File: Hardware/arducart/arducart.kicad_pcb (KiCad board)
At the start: 2 copper layers, 53 x 39.2 mm, 11 parts, among them J2 AVR-ISP-6

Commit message: First routing
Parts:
- R2, R3, R4, R5, R6, R7, R8: moved to B.Cu
- moved R3 26.2 mm to (146.9, 78.0), turned to 90 degrees
- moved R2 24.1 mm to (141.9, 83.8), turned to -90 degrees
- moved R4 23.5 mm to (144.4, 78.0), turned to 90 degrees
- moved R5 21.2 mm to (141.9, 78.0), turned to 90 degrees
- moved R1 20.5 mm to (118.4, 88.8), turned to -90 degrees
- moved R6 19.7 mm to (139.3, 78.0), turned to 90 degrees
- moved R7 18.9 mm to (139.3, 83.8), turned to -90 degrees
- moved R8 15.4 mm to (134.2, 83.8), turned to -90 degrees
- moved J2 3.23 mm to (161.7, 82.1)
- moved U1 1.01 mm to (141.9, 80.9), turned to 90 degrees
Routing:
- net GND: track 0.00 -> 157.3 mm, vias 0 -> 5
- net VCC: track 0.00 -> 84.2 mm, vias 0 -> 1
- net ISP_SCK: track 0.00 -> 80.4 mm
- net ISP_MOSI: track 0.00 -> 71.7 mm
- net BTN_UP: track 0.00 -> 45.8 mm
- net BTN_DOWN: track 0.00 -> 41.0 mm, vias 0 -> 1
- net ISP_RST: track 0.00 -> 40.3 mm
- net BTN_RIGHT: track 0.00 -> 32.3 mm, vias 0 -> 1
- net BTN_LEFT: track 0.00 -> 32.3 mm
- net SPI_CS: track 0.00 -> 32.0 mm, vias 0 -> 2
- net SCREEN_DC: track 0.00 -> 28.3 mm
- net BUZZER: track 0.00 -> 28.0 mm
- net Net-(J1-BTN_MENU1): track 0.00 -> 25.8 mm, vias 0 -> 2
- net SCREEN_RESET: track 0.00 -> 23.6 mm
- net BTN_B: track 0.00 -> 21.1 mm, vias 0 -> 2
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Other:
- board size 53 x 39.2 mm -> 53 x 36.2 mm

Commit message: Finish PCB design
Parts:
- moved J2 1.50 mm to (160.9, 80.9)
- moved R2 1.27 mm to (141.9, 82.5)
- moved R3 1.27 mm to (146.9, 76.7)
- moved R4 1.27 mm to (144.4, 76.7)
- moved R5 1.27 mm to (141.9, 76.7)
- moved R6 1.27 mm to (139.3, 76.7)
- moved R8 1.27 mm to (134.2, 82.6)
- moved U1 1.27 mm to (141.9, 79.6)
- moved R1 1.27 mm to (118.4, 87.5)
- moved R7 1.27 mm to (139.3, 82.5)
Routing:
- net BTN_A: track 19.1 -> 43.8 mm, vias 0 -> 1
- net BTN_B: track 21.1 -> 41.1 mm, vias 2 -> 5
- net ISP_MOSI: track 71.7 -> 78.7 mm
- net GND: track 157.3 -> 164.1 mm
- net ISP_SCK: track 80.4 -> 83.9 mm
- net BTN_UP: track 45.8 -> 48.8 mm
- net BTN_LEFT: track 32.3 -> 35.1 mm
- net SCREEN_RESET: track 23.6 -> 25.9 mm
- net SCREEN_DC: track 28.3 -> 30.2 mm
- net BTN_RIGHT: track 32.3 -> 34.1 mm
- net ISP_MISO: track 21.1 -> 19.5 mm
- net Net-(J1-BTN_MENU1): track 25.8 -> 27.1 mm
- net BUZZER: track 28.0 -> 29.2 mm
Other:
- board size 53 x 36.2 mm -> 53 x 37.5 mm
- board text added: "1"
- board text added: "30"
- board text added: "ArduCard v0.1"
- board text added: "MISO"
- board text added: "MOSI"
- board text added: "RST"
- board text added: "SCK"
- board text added: "VCC"

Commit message: Add logo on PCBs
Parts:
- added REF**: Logo, carts:Logo, F.Cu at (122.8, 75.8)
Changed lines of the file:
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@@
 		)
+	)
+	(footprint "carts:Logo"
+		(layer "F.Cu")
+		(at 122.75 75.75)
+		(property "Reference" "REF**"
+			(at 0 -5.08 0)
+			(unlocked yes)
+			(layer "F.SilkS")
+			(hide yes)
+			(effects
+				(font
+					(size 1 1)
+					(thickness 0.1)
+				)
+			)
+		)
+		(property "Value" "Logo"
+			(at 0 5.08 0)
+			(unlocked yes)
+			(layer "F.Fab")
+			(hide yes)
+			(effects
+				(font
+					(size 1 1)
+					(thickness 0.15)
+				)
+			)
+		)
+		(property "Datasheet" ""
+			(at 0 0 0)
+			(unlocked yes)
+			(layer "F.Fab")
+			(hide yes)
+			(effects
+				(font
+					(size 1 1)
+					(thickness 0.15)
+				)
+			)
+		)
+		(property "Description" ""
+			(at 0 0 0)
+			(unlocked yes)
+			(layer "F.Fab")
+			(hide yes)
+			(effects
+				(font
+					(size 1 1)
+					(thickness 0.15)
+				)
+			)
+		)
+		(attr smd)
+		(fp_line
+			(start -1 -2.75)
+			(end 0 -2.75)
+			(stroke
+				(width 1)
+				(type default)
+			)
+			(layer "F.SilkS")
+		)
+		(fp_line
+			(start -1 -0.25)
+			(end -1 0.5)
+			(stroke
+				(width 0.5)
+				(type default)
+			)
+			(layer "F.SilkS")
+		)
+		(fp_line
+			(start 1.5 1.25)
+			(end 1.5 -2.75)
+			(stroke
+				(width 1)
+				(type default)
+			)
+			(layer "F.SilkS")
+		)
+		(fp_line
+			(start 2 -0.75)
+			(end -0.5 -0.75)
+			(stroke
+				(width 0.5)
+				(type default)
+			)
+			(layer "F.SilkS")
+		)
+		(fp_line
+			(start 3.5 -2.75)
+			(end 1.5 -2.75)
+			(stroke
+				(width 1)
+				(type default)
+			)
+			(layer "F.SilkS")
+		)
+		(fp_line
+			(start 3.5 -0.75)
+			(end 1.5 -0.75)
+			(stroke
+				(width 1)
+				(type default)
+			)
+			(layer "F.SilkS")
+		)
+		(fp_line
+			(start 3.5 1.25)
+			(end 1.5 1.25)
+			(stroke
+				(width 1)
+				(type default)
+			)
+			(layer "F.SilkS")
+		)
+		(fp_line
+			(start 3.5 2.75)
+			(end -1 2.75)
+			(stroke
+				(width 1)
+				(type default)
+			)
+			(layer "F.SilkS")
+		)
+		(fp_arc
+			(start -1 2.75)
+			(mid -3.75 0)
+			(end -1 -2.75)
+			(stroke
+				(width 1)
+				(type default)
+			)
+			(layer "F.SilkS")
+		)
+		(fp_circle
+			(center -1 -0.75)
+			(end -0.5 -0.75)
+			(stroke
+				(width 0.5)
+				(type solid)
+			)
+			(fill no)
+			(layer "F.SilkS")
+		)
+		(fp_circle
+			(center -1 1)
+			(end -0.5 1)
+			(stroke
+				(width 0.5)
+				(type solid)
+			)
+			(fill no)
+			(layer "F.SilkS")
+		)
+		(fp_rect
+			(start -4.25 -3.25)
+			(end 4 3.25)
+			(stroke
+				(width 0.1)
+				(type solid)
+			)
+			(fill no)
+			(layer "F.CrtYd")
+		)
+		(fp_text user "${REFERENCE}"
+			(at -0.25 -4.25 0)
+			(unlocked yes)
+			(layer "F.Fab")
+			(effects
+				(font
+					(size 1 1)
+					(thickness 0.15)
+				)
+			)
+		)
+		(embedded_fonts no)
 	)
 	(footprint "carts:Edge_Connector"

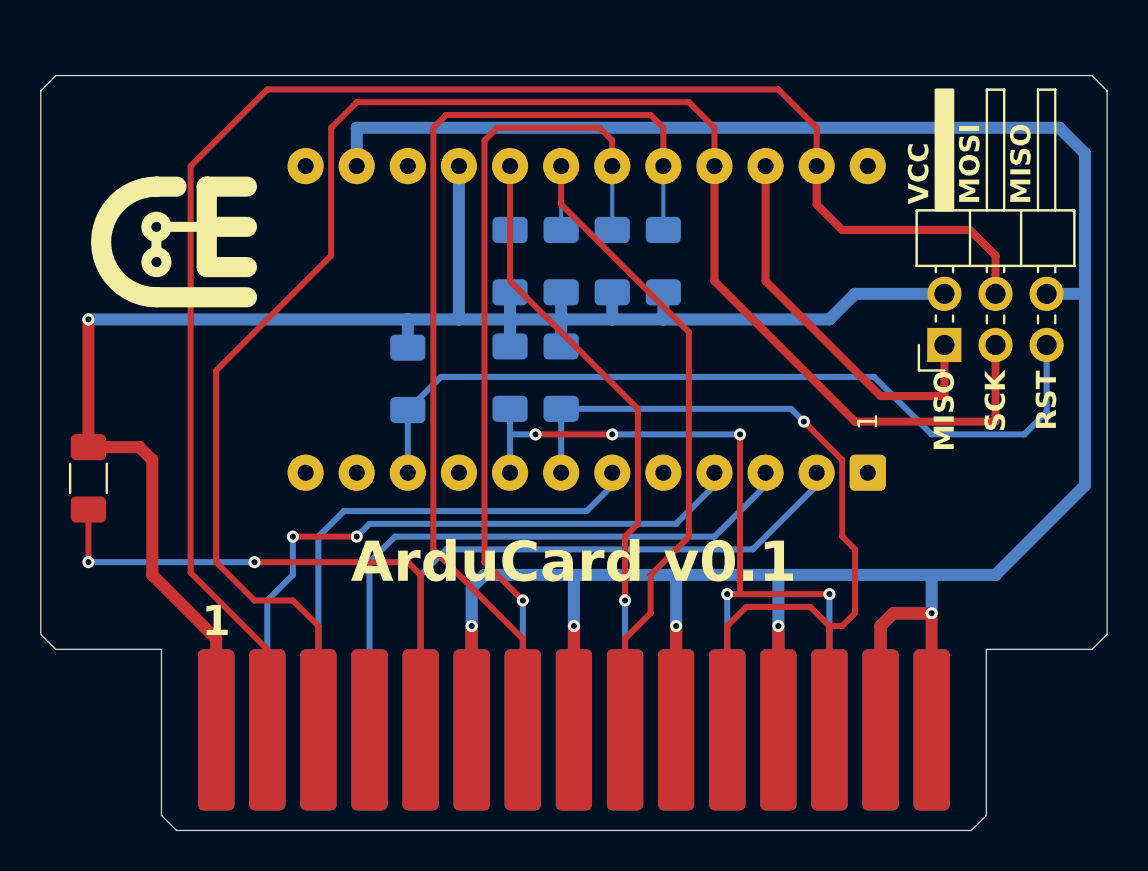
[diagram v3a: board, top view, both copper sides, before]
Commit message: Add holes, add space for cartrige case
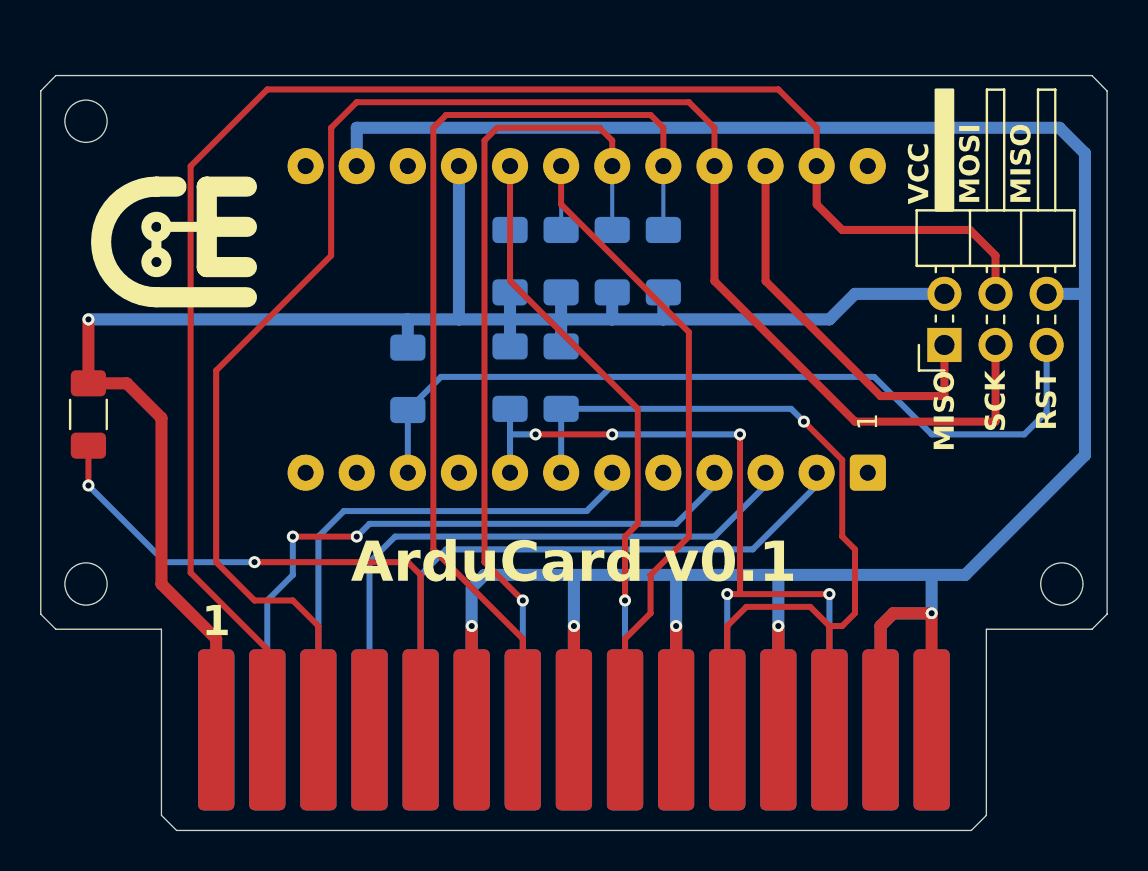
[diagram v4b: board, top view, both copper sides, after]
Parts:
- added REF**: MountingHole_2.1mm, MountingHole:MountingHole_2.1mm, F.Cu at (118.2, 92.8)
- added REF**: MountingHole_2.1mm, MountingHole:MountingHole_2.1mm, F.Cu at (118.2, 69.8)
- added REF**: MountingHole_2.1mm, MountingHole:MountingHole_2.1mm, F.Cu at (166.8, 92.8)
- moved R1 3.17 mm to (118.4, 84.3)
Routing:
- net Net-(J1-BTN_MENU1): track 27.1 -> 28.0 mm
- net GND: track 164.1 -> 163.2 mm
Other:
- outline, holes or cut-outs redrawn

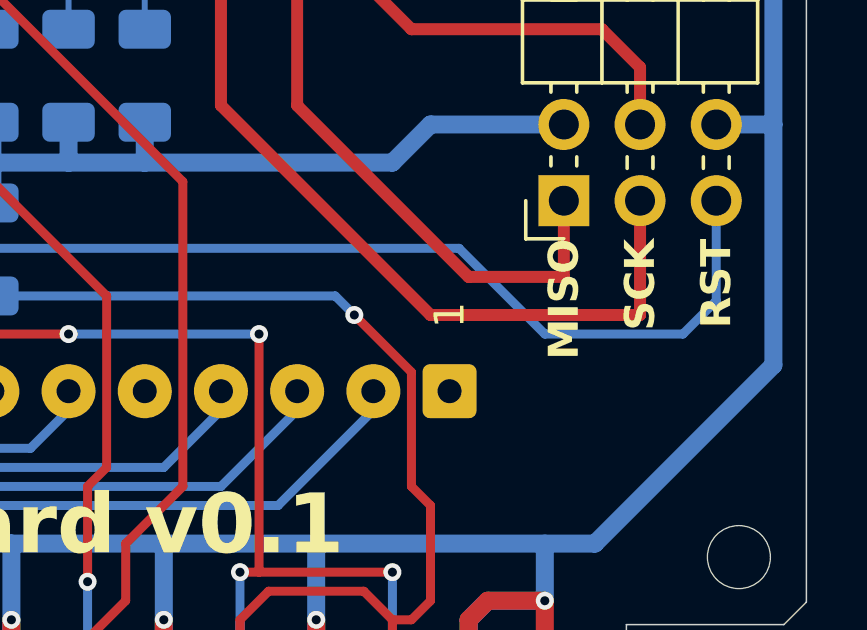
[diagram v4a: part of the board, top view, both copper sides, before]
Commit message: Fixes to comply to design rules
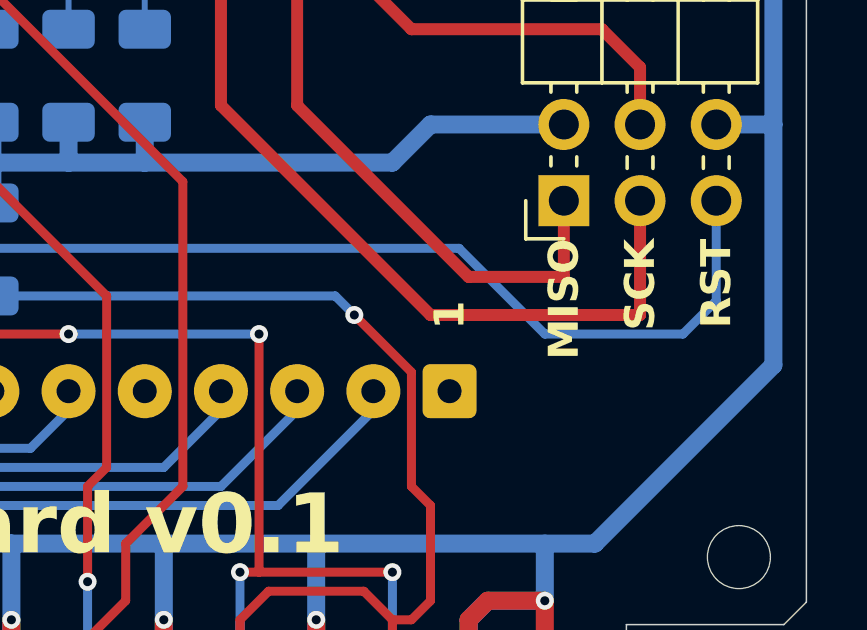
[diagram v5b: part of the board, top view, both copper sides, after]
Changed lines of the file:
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@@
 	)
 	(setup
+		(stackup
+			(layer "F.SilkS"
+				(type "Top Silk Screen")
+			)
+			(layer "F.Paste"
+				(type "Top Solder Paste")
+			)
+			(layer "F.Mask"
+				(type "Top Solder Mask")
+				(thickness 0.01)
+			)
+			(layer "F.Cu"
+				(type "copper")
+				(thickness 0.035)
+			)
+			(layer "dielectric 1"
+				(type "core")
+				(thickness 1.51)
+				(material "FR4")
+				(epsilon_r 4.5)
+				(loss_tangent 0.02)
+			)
+			(layer "B.Cu"
+				(type "copper")
+				(thickness 0.035)
+			)
+			(layer "B.Mask"
+				(type "Bottom Solder Mask")
+				(thickness 0.01)
+			)
+			(layer "B.Paste"
+				(type "Bottom Solder Paste")
+			)
+			(layer "B.SilkS"
+				(type "Bottom Silk Screen")
+			)
+			(copper_finish "None")
+			(dielectric_constraints no)
+		)
 		(pad_to_mask_clearance 0)
 		(allow_soldermask_bridges_in_footprints no)
@@
 		(sheetfile "arducart.kicad_sch")
 		(attr through_hole)
-		(fp_poly
-			(pts
-				(xy -9.274999 -16.8) (xy 9.274999 -16.8) (xy 9.274999 16.8) (xy -9.274999 16.8)
-			)
+		(fp_rect
+			(start -9.275 -16.8)
+			(end 9.275 16.8)
 			(stroke
 				(width 0.1)
@@
 				(font
 					(size 1 1)
-					(thickness 0.1)
+					(thickness 0.2)
+					(bold yes)
 				)
 			)
@@
 			(layer "F.SilkS")
 		)
-		(fp_rect
-			(start -4.25 -3.25)
-			(end 4 3.25)
-			(stroke
-				(width 0.1)
-				(type solid)
-			)
-			(fill no)
-			(layer "F.CrtYd")
-		)
 		(fp_text user "${REFERENCE}"

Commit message: Tune export settings
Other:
- board text added: "GND"
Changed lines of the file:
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@@
 			(plot_on_all_layers_selection 0x00000000_00000000_00000000_00000000)
 			(disableapertmacros no)
-			(usegerberextensions no)
+			(usegerberextensions yes)
 			(usegerberattributes yes)
 			(usegerberadvancedattributes yes)
@@
 			(sketchdnponfab yes)
 			(crossoutdnponfab yes)
-			(subtractmaskfromsilk no)
+			(subtractmaskfromsilk yes)
 			(outputformat 1)
 			(mirror no)
-			(drillshape 1)
+			(drillshape 0)
 			(scaleselection 1)
-			(outputdirectory "")
+			(outputdirectory "../gerber/")
 		)
 	)
@@
 		)
 	)
-	(gr_text "MISO"
+	(gr_text "GND"
 		(at 164.725 73.885 90)
 		(layer "F.SilkS")
